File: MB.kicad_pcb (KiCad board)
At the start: 4 copper layers, 90.2 x 94.1 mm, 48 parts, among them J100 VCC INPUT, J101 SWITCH ON/OFF, J102 JUMPER ON/OFF TEST, J103 FAN VOLTAGE, J200 DOOR_OUTPUT, J300 MCP_EXTERNAL, J301 CAN_INPUT, K200 HF49FD/005-1H12T, Q100 WST4045, Q200 2N3904, U100 LM2596S-5, U101 AMS1117-3.3, U200 MEGA_PRO_EMBED_CH340G_{slash}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, U300 MCP2515-xSO, U301 TJA1050, Y300 8MHz

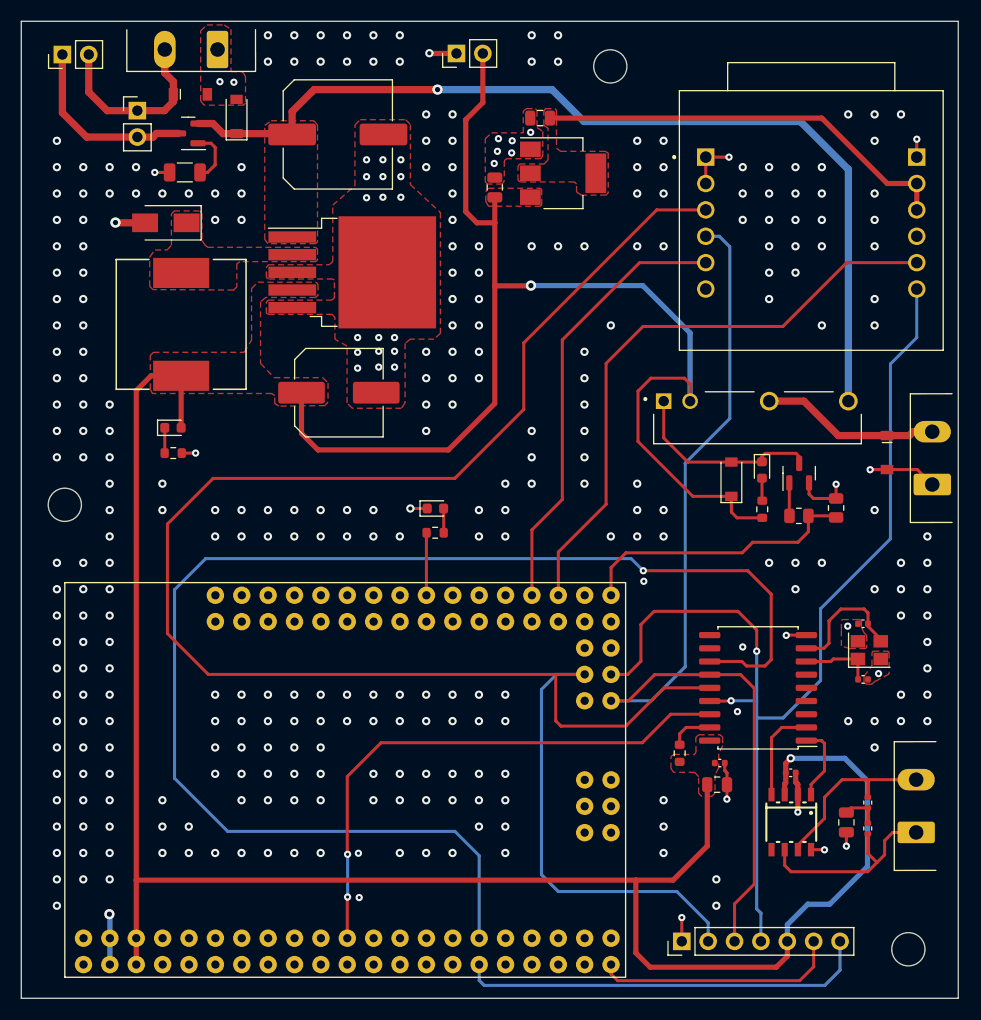
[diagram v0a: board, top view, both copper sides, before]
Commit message: added component labels
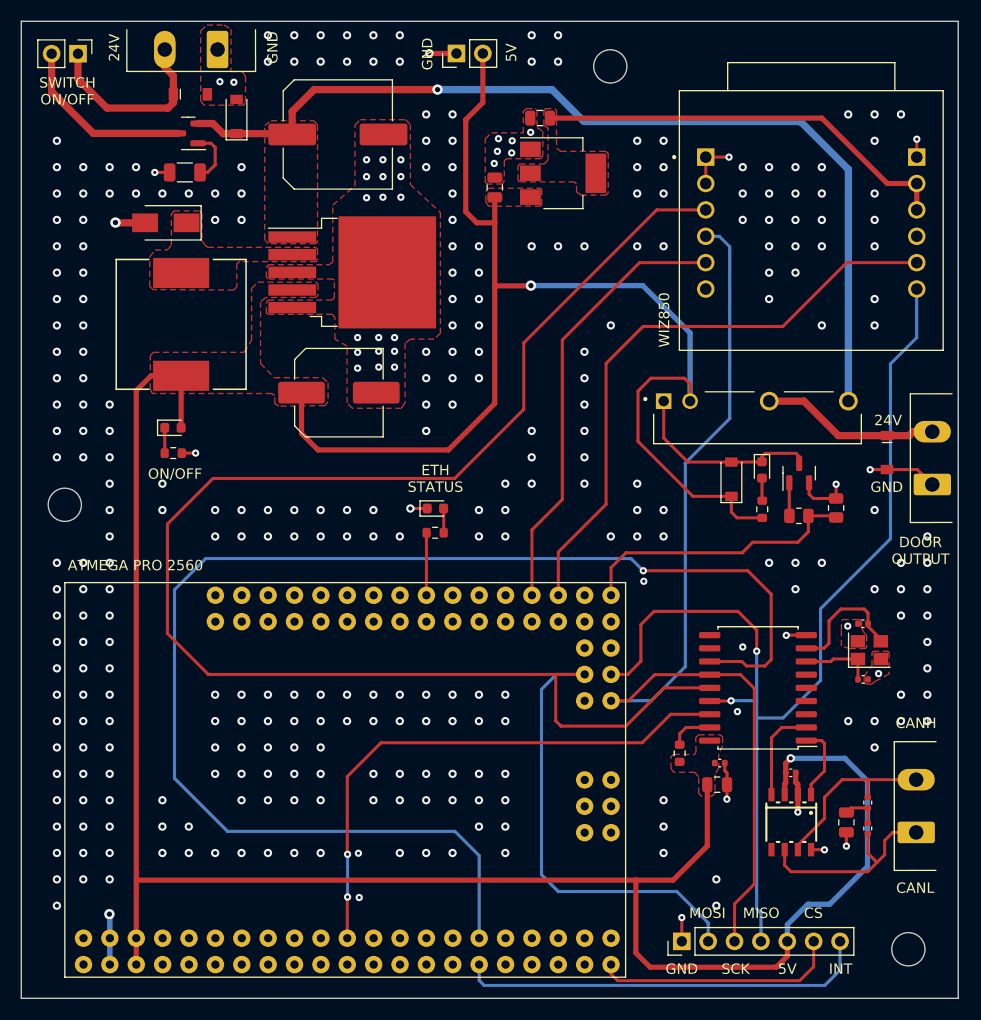
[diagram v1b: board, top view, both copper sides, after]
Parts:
- removed J102: JUMPER ON/OFF TEST, Connector_PinHeader_2.54mm:PinHeader_1x02_P2.54mm_Vertical
- moved J101 7.92 mm to (134.1, 32.3), turned to -90 degrees
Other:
- board text added: "24V"
- board text added: "5V"
- board text added: "ATMEGA PRO 2560"
- board text added: "CANH"
- board text added: "CANL"
- board text added: "CS"
- board text added: "DOOR OUTPUT"
- board text added: "ETH STATUS"
- board text added: "GND"
- board text added: "INT"
- board text added: "MISO"
- board text added: "MOSI"
- board text added: "ON/OFF"
- board text added: "SCK"
- board text added: "SWITCH ON/OFF"
- board text added: "WIZ850"

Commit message: added BOM, Gerber and modified a few footprints
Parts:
- added TP100: TestPoint, TestPoint:TestPoint_Pad_D2.0mm, F.Cu at (131.3, 44.2)
- added TP101: TestPoint, TestPoint:TestPoint_Pad_D2.0mm, F.Cu at (170.5, 31.9)
- added TP102: TestPoint, TestPoint:TestPoint_Pad_D2.0mm, F.Cu at (177.6, 31.9)
- added TP103: TestPoint, TestPoint:TestPoint_Pad_D2.0mm, F.Cu at (174.1, 31.9)
- added TP104: TestPoint, TestPoint:TestPoint_Pad_D2.0mm, F.Cu at (131.2, 48.3)
- added TP300: TestPoint, TestPoint:TestPoint_Pad_D2.0mm, F.Cu at (210.2, 96.6)
- added TP301: TestPoint, TestPoint:TestPoint_Pad_D2.0mm, F.Cu at (211.4, 114.4)
- C100: value 100u -> 330u
- C101: footprint Capacitor_SMD:C_Elec_8x10.2 -> Capacitor_SMD:CP_Elec_10x10.5
- C300: footprint Capacitor_SMD:C_0805_2012Metric -> Capacitor_SMD:C_0603_1608Metric
- C301, C304: value 0.1u -> 100n
- D202: value 1N4007W -> SM4007PL; footprint Diode_SMD:D_SOD-123 -> Jose_:SOD_123FL
- D203: value LED_HEADBOARD -> LED_DOOR
- Q200: value 2N3904 -> MMBT3904
- R202, R203: footprint Resistor_SMD:R_0805_2012Metric -> Resistor_SMD:R_0603_1608Metric
- moved J103 49.6 mm to (131.6, 63.0), turned to 0 degrees
- moved J101 5.36 mm to (131.9, 37.1), turned to 0 degrees
- moved D101 1.88 mm to (149.4, 40.2), turned to -90 degrees
- moved H4 1.30 mm to (215.0, 119.4)
- moved Q100 0.87 mm to (143.9, 39.8)
- moved D202 0.74 mm to (196.3, 73.3)
- moved R203 0.56 mm to (207.6, 76.2)
- moved R202 0.37 mm to (203.4, 77.1)
- moved Q200 0.36 mm to (203.6, 73.0)
- moved R201 0.28 mm to (199.9, 76.4)
- moved R100 0.24 mm to (144.2, 43.8)
- moved D203 0.18 mm to (199.9, 72.5)
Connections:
- D101 pad 2: GND -> Net-(D101-Pad2)
- Q100 pad 1: Net-(Q100-Pad1) -> Net-(D101-Pad2)
- R100 pad 1: Net-(Q100-Pad1) -> Net-(D101-Pad2)
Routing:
- net +5V: track 302.9 -> 312.2 mm
- net Net-(D101-Pad2): track 0.00 -> 8.52 mm
- net /POWER/V_INPUT: track 18.5 -> 26.1 mm
- net +3V3: track 40.5 -> 47.8 mm
- net GND: track 47.4 -> 54.7 mm, vias 342 -> 322
- net Net-(J101-Pad2): track 17.5 -> 11.2 mm
- net /CAN/CANH: track 17.4 -> 23.5 mm
- net Net-(Q100-Pad1): track 5.26 -> 0.00 mm
- net /CAN/CANL: track 19.9 -> 25.0 mm
- net +24V: track 91.6 -> 92.8 mm
- net /MCU/COIL_1: track 19.0 -> 19.6 mm
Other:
- board text added: "3.3V"

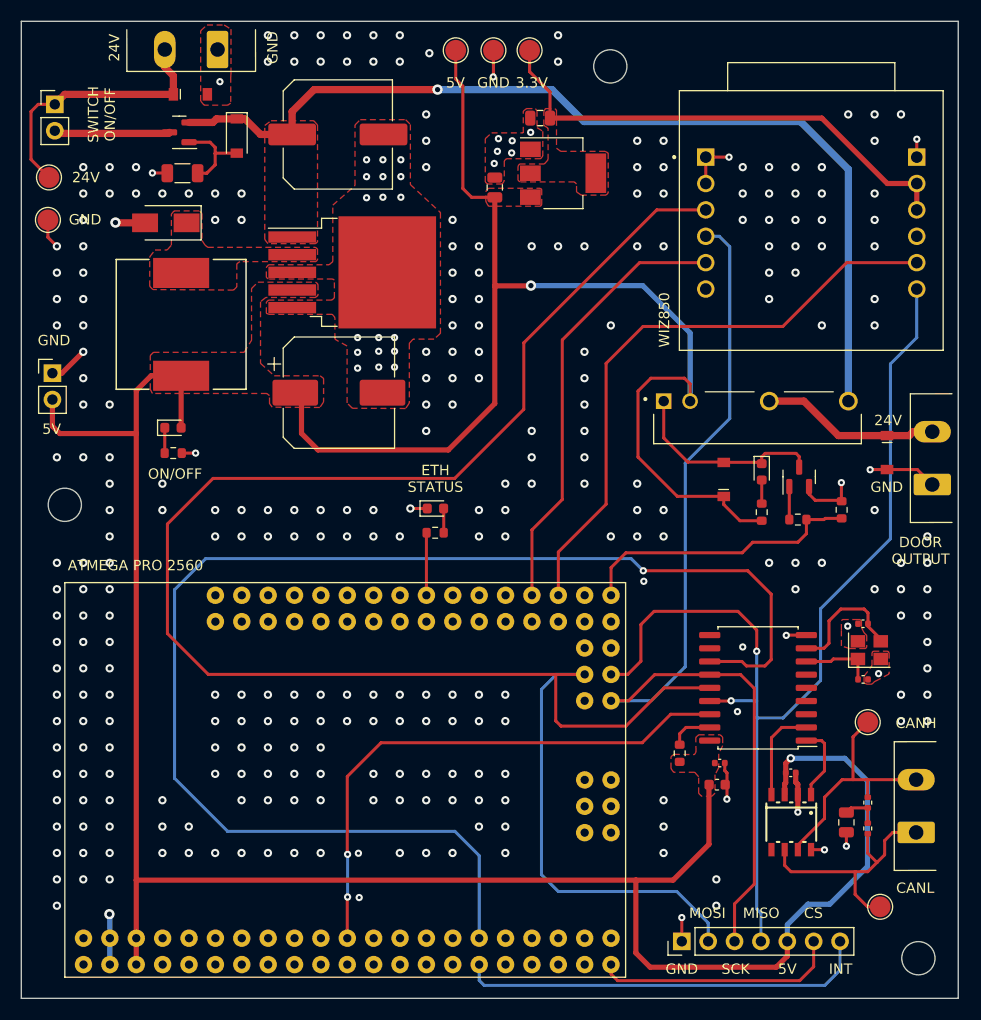
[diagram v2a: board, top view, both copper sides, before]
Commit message: change names and move WIZ850 position
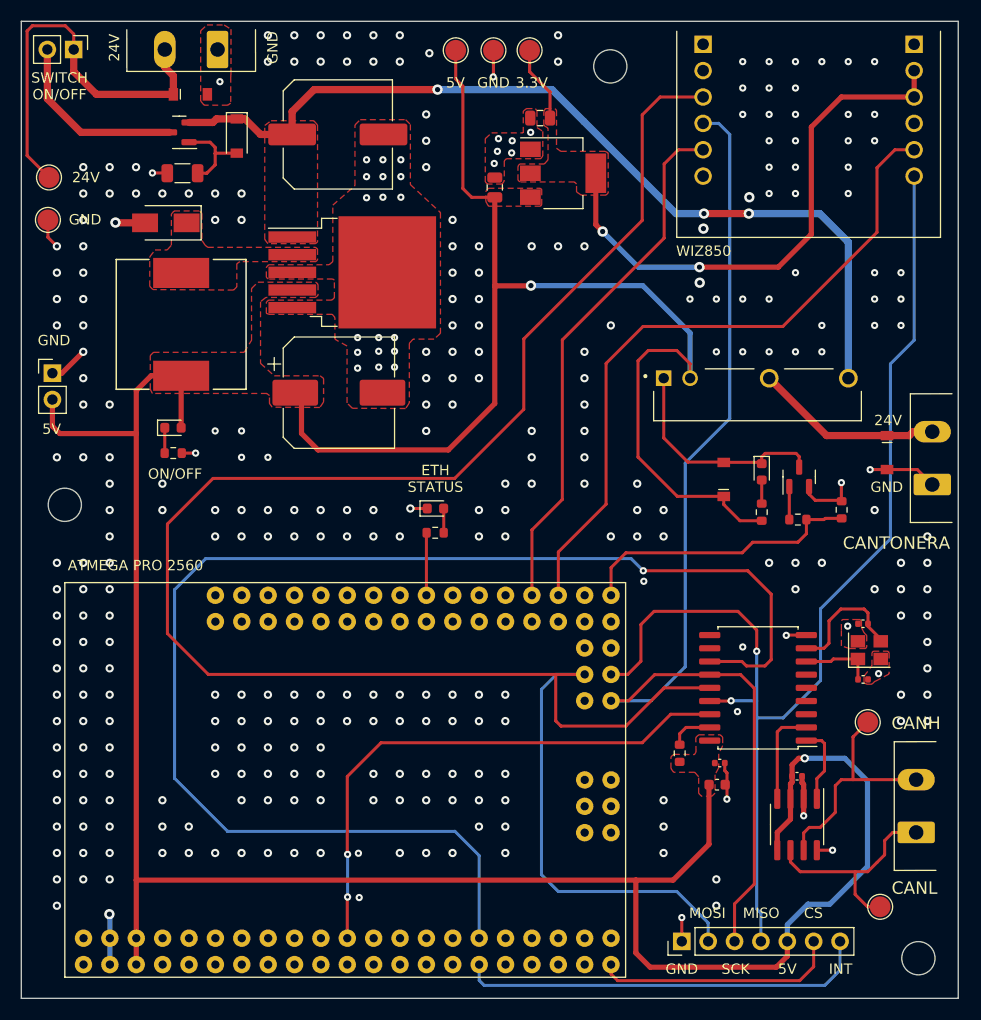
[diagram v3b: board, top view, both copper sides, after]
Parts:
- removed C305: 4n7, Capacitor_SMD:C_0805_2012Metric
- removed R301, R302: 60, Resistor_SMD:R_0402_1005Metric
- U301: value TJA1050 -> TJA1051T-3; footprint TJA1050T:SOT96-1 -> Package_SO:SOIC-8_3.9x4.9mm_P1.27mm
- moved H200 10.9 mm to (204.2, 36.1)
- moved J101 5.59 mm to (133.7, 31.9), turned to -90 degrees
- moved K200 2.21 mm to (199.5, 65.1)
- moved C304 0.69 mm to (203.4, 101.8)
- moved U301 0.60 mm to (203.4, 106.5), turned to -90 degrees
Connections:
- U301 pad 5: unconnected-(U301-Pad5) -> +5V
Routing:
- net /POWER/V_INPUT: track 26.1 -> 38.8 mm
- net +3V3: track 47.8 -> 60.0 mm, vias 0 -> 2
- net SPI_SCK: track 94.0 -> 105.1 mm
- net SPI_MISO: track 103.2 -> 114.0 mm
- net SPI_MOSI: track 183.9 -> 194.3 mm
- net ETH_CS: track 42.7 -> 51.1 mm
- net ETH_RST: track 58.2 -> 66.1 mm
- net GND: track 54.7 -> 47.0 mm, vias 322 -> 331
- net Net-(J101-Pad2): track 11.2 -> 17.9 mm
- net +24V: track 92.8 -> 86.5 mm, vias 1 -> 3
- net +5V: track 312.2 -> 318.1 mm
- net /CAN/CANL: track 25.0 -> 21.1 mm
- net Net-(C305-Pad1): track 3.71 -> 0.00 mm
- net /MCU/COIL_1: track 19.6 -> 21.8 mm
- net /CAN/CANH: track 23.5 -> 22.3 mm
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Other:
- board text added: "0.2000 mm / 0.2000 mm"
- board text added: "0.3000 mm"
- board text added: "1.6134 mm"
- board text added: "4"
- board text added: "90.2208 mm x 94.0816 mm"
- board text added: "BOARD CHARACTERISTICS"
- board text added: "Board Thickness:"
- board text added: "Board overall dimensions:"
- board text added: "CANTONERA"
- board text added: "Castellated pads:"
- board text added: "Copper Finish:"
- board text added: "Copper Layer Count:"
- board text added: "Edge card connectors:"
- board text added: "Impedance Control:"
- board text added: "Min hole diameter:"
- board text added: "Min track/spacing:"
- board text added: "No"
- board text added: "None"
- board text added: "Plated Board Edge:"
- board text removed: "DOOR OUTPUT"

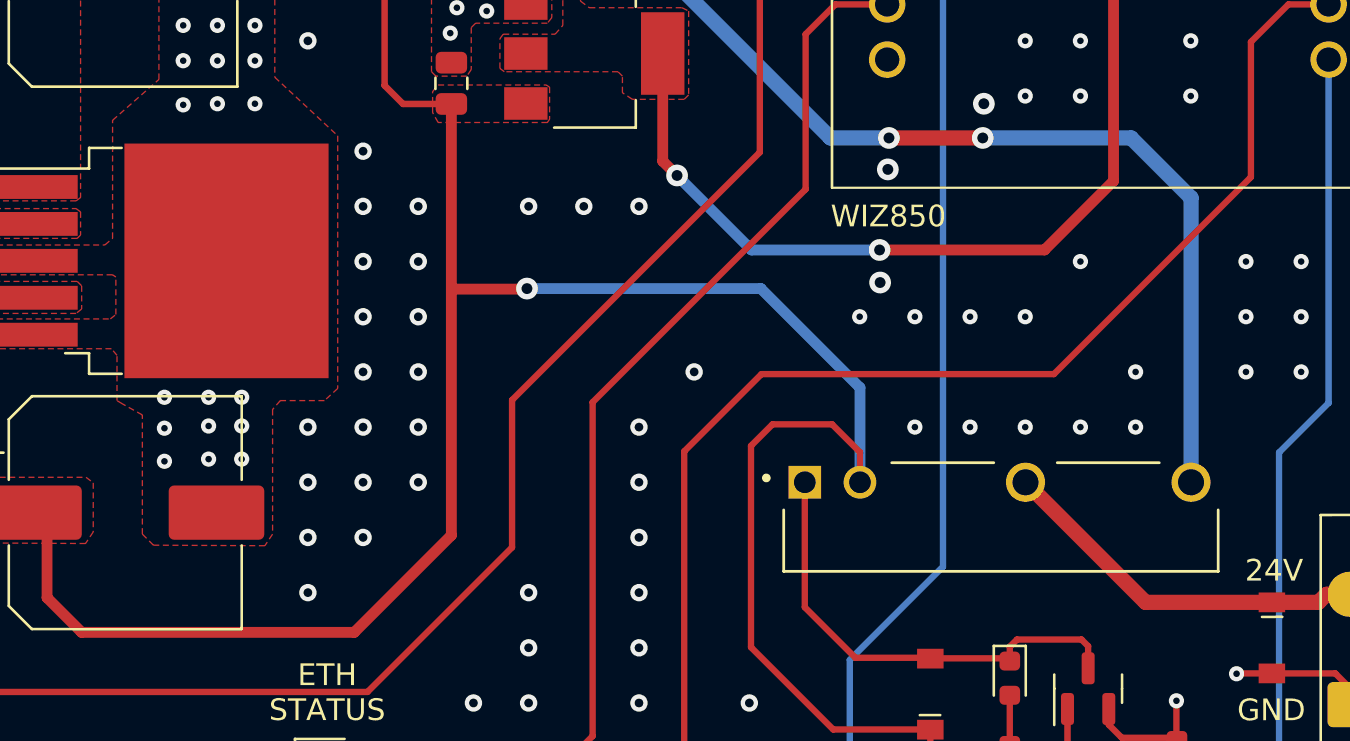
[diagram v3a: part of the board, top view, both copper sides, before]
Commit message: added vias in thermal pad and change relay footprint
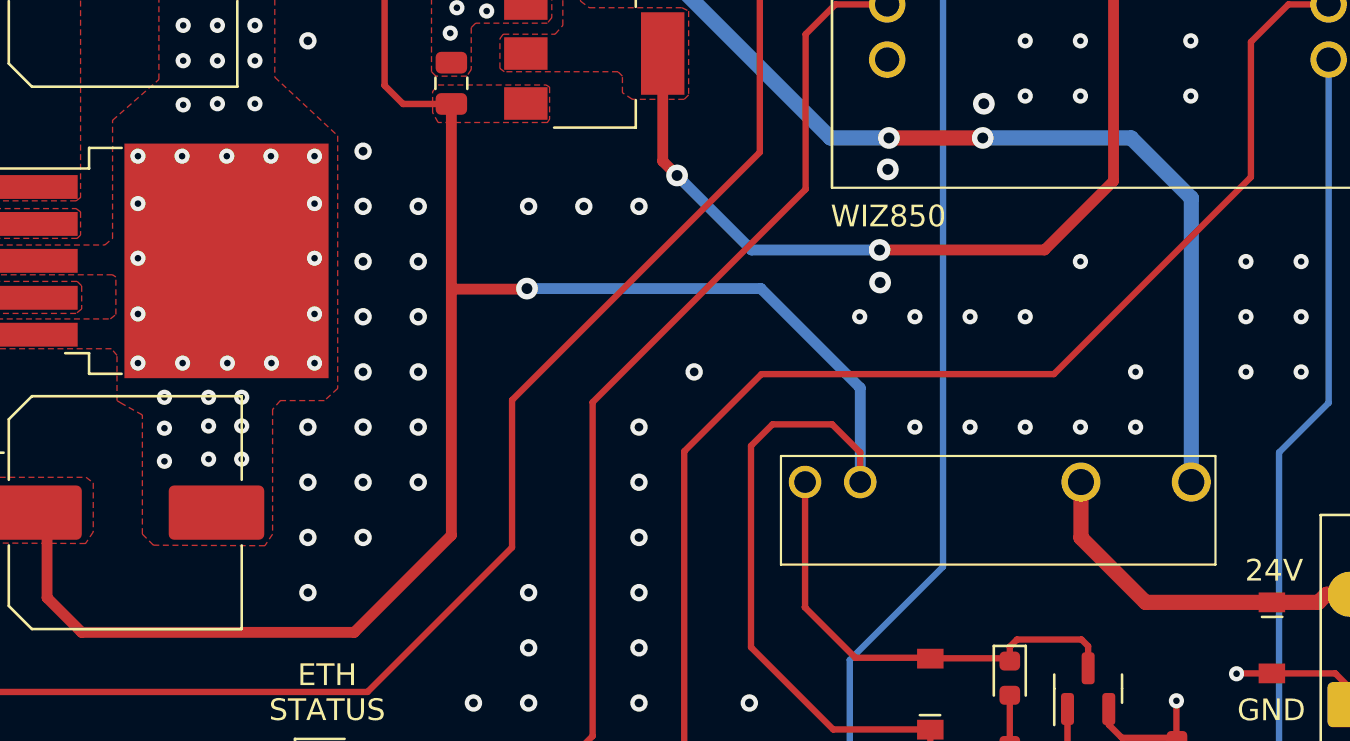
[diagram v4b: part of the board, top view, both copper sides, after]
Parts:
- K200: footprint HF49_RELAY:RELAY_HF49FD_005-1H12T -> HF49FD_005-1H11F:HF49FD0051H11F
- moved K200 0.67 mm to (199.4, 64.4), turned to 180 degrees
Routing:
- net /MCU/RELAY_24V: track 18.1 -> 17.1 mm
- net GND: vias 331 -> 347
